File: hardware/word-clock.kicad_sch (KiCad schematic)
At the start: 0 parts

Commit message: feat(hardware): schematic v0 - erc clean, ready for pcb layout
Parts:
- added C2, C3, C4, C5, C6: 100nF, symbol Device:C
- added C7: 1000µF / 10V, symbol Device:C_Polarized
- added ESP32: ESP32 DevKit V1, symbol Connector_Generic:Conn_02x19_Odd_Even
- added J_AMP1: MAX98357A breakout, symbol Connector_Generic:Conn_01x07
- added J_LED1: WS2812B strip, symbol Connector_Generic:Conn_01x03
- added J_RTC1: DS3231 ZS-042, symbol Connector_Generic:Conn_01x06
- added J_SD1: HW-125 microSD, symbol Connector_Generic:Conn_01x06
- added J_USB1: USB-C breakout (Cermant 16P), symbol Connector_Generic:Conn_01x04
- added R1: Resistor 300 ohm, symbol Device:R
- added SW1: Hour, symbol Switch:SW_Push
- added SW2: Minute, symbol Switch:SW_Push
- added SW3: Audio, symbol Switch:SW_Push
- added U2: 74HC245, symbol 74xx:74HC245
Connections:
- new net +3V3: C2.1, C5.1, ESP32.3V3, J_RTC1.5 (VCC)
- new net +5V: C3.1, C4.2, C6.2, C7.1, ESP32.VIN (Pin_19), J_AMP1.7 (VIN), J_LED1.1 (+5V), J_SD1.2 (VCC), J_USB1.1 (VBUS), U2.1 (A->B), U2.20 (VCC)
- new net BTN_AUDIO: ESP32.D14 (Pin_12), SW3.1
- new net BTN_HOUR: ESP32.D32 (Pin_7), SW1.1
- new net BTN_MINUTE: ESP32.D33 (Pin_8), SW2.1
- new net GND: C2.2, C3.2, C4.1, C5.2, C6.1, C7.2, ESP32.GND (Pin_26), J_AMP1.6 (GND), J_LED1.2 (GND), J_RTC1.6 (GND), J_SD1.1 (GND), J_USB1.2 (GND), SW1.2, SW2.2, SW3.2, U2.10 (GND), U2.19 (CE), U2.3 (A1), U2.4 (A2), U2.5 (A3), U2.6 (A4), U2.7 (A5), U2.8 (A6), U2.9 (A7)
- new net I2C_SCL: ESP32.D22 (Pin_22), J_RTC1.3 (SCL)
- new net I2C_SDA: ESP32.D21 (Pin_25), J_RTC1.4 (SDA)
- new net I2S_BCLK: ESP32.D26 (Pin_10), J_AMP1.2 (BCLK)
- new net I2S_DIN: ESP32.D27 (Pin_11), J_AMP1.3 (DIN)
- new net I2S_LRC: ESP32.D25 (Pin_9), J_AMP1.1 (LRC)
- new net LED_DATA_3V3: ESP32.D13 (Pin_15), U2.2 (A0)
- new net LED_DATA_5V: R1.1, U2.18 (B0)
- new net LED_DATA_OUT: J_LED1.3 (DATA), R1.2
- new net SD_CS: ESP32.D5 (Pin_29), J_SD1.6 (CS)
- new net SD_MISO: ESP32.D19 (Pin_27), J_SD1.3 (MISO)
- new net SD_MOSI: ESP32.D23 (Pin_21), J_SD1.4 (MOSI)
- new net SD_SCK: ESP32.D18 (Pin_28), J_SD1.5 (SCK)
- no-connect marks 0 -> 33

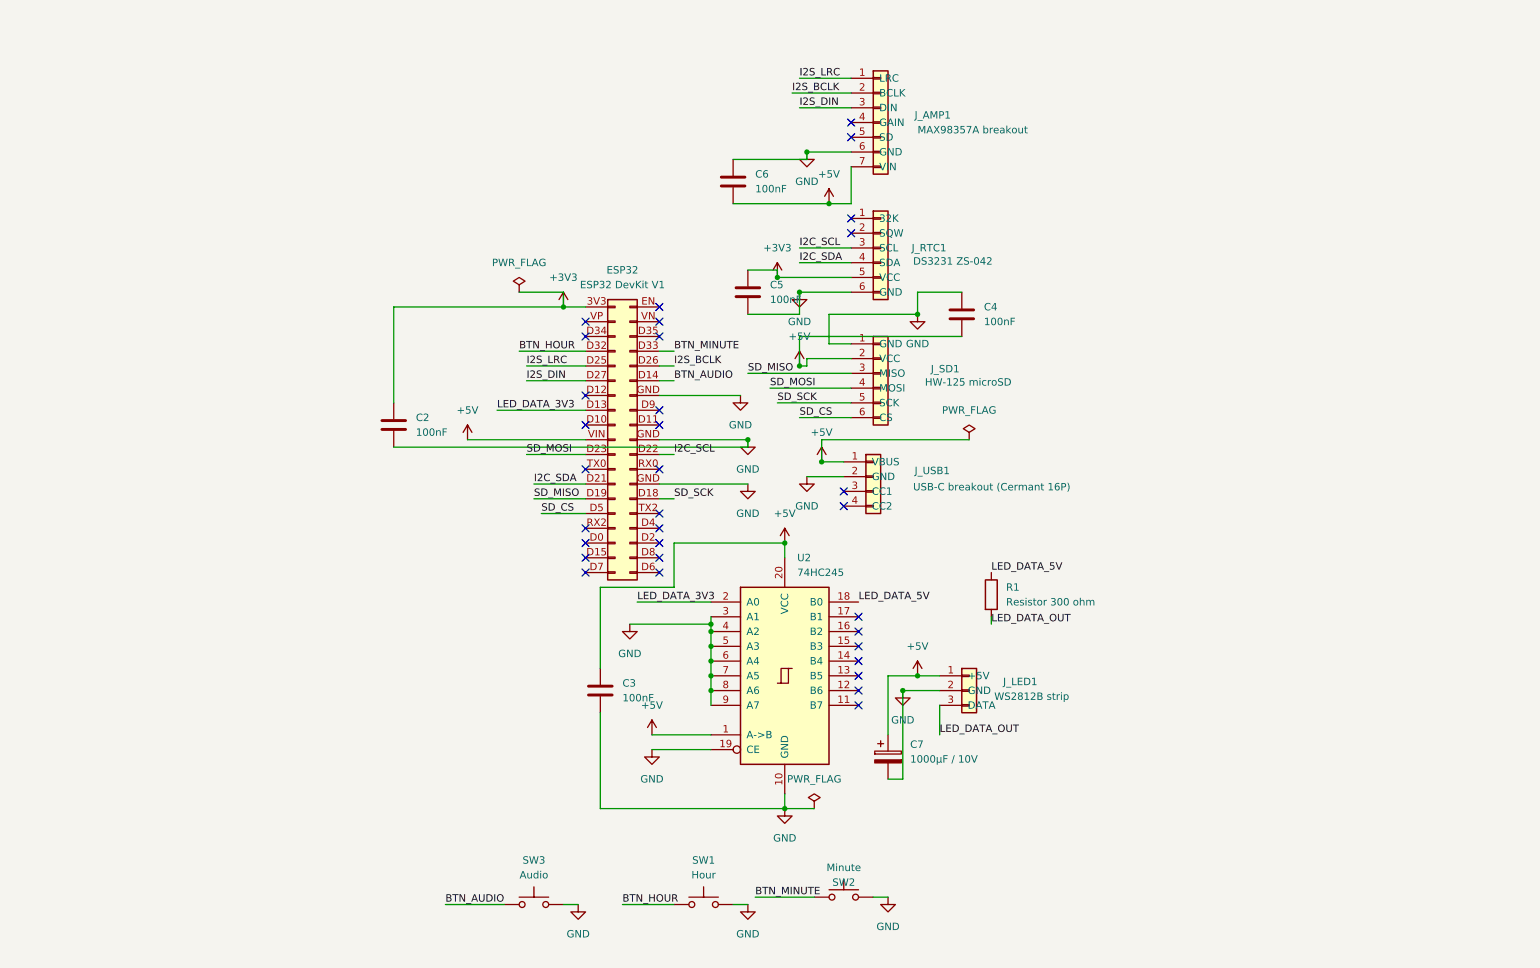
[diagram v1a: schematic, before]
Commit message: feat(hardware): schematic — 35 smd ws2812b leds chained
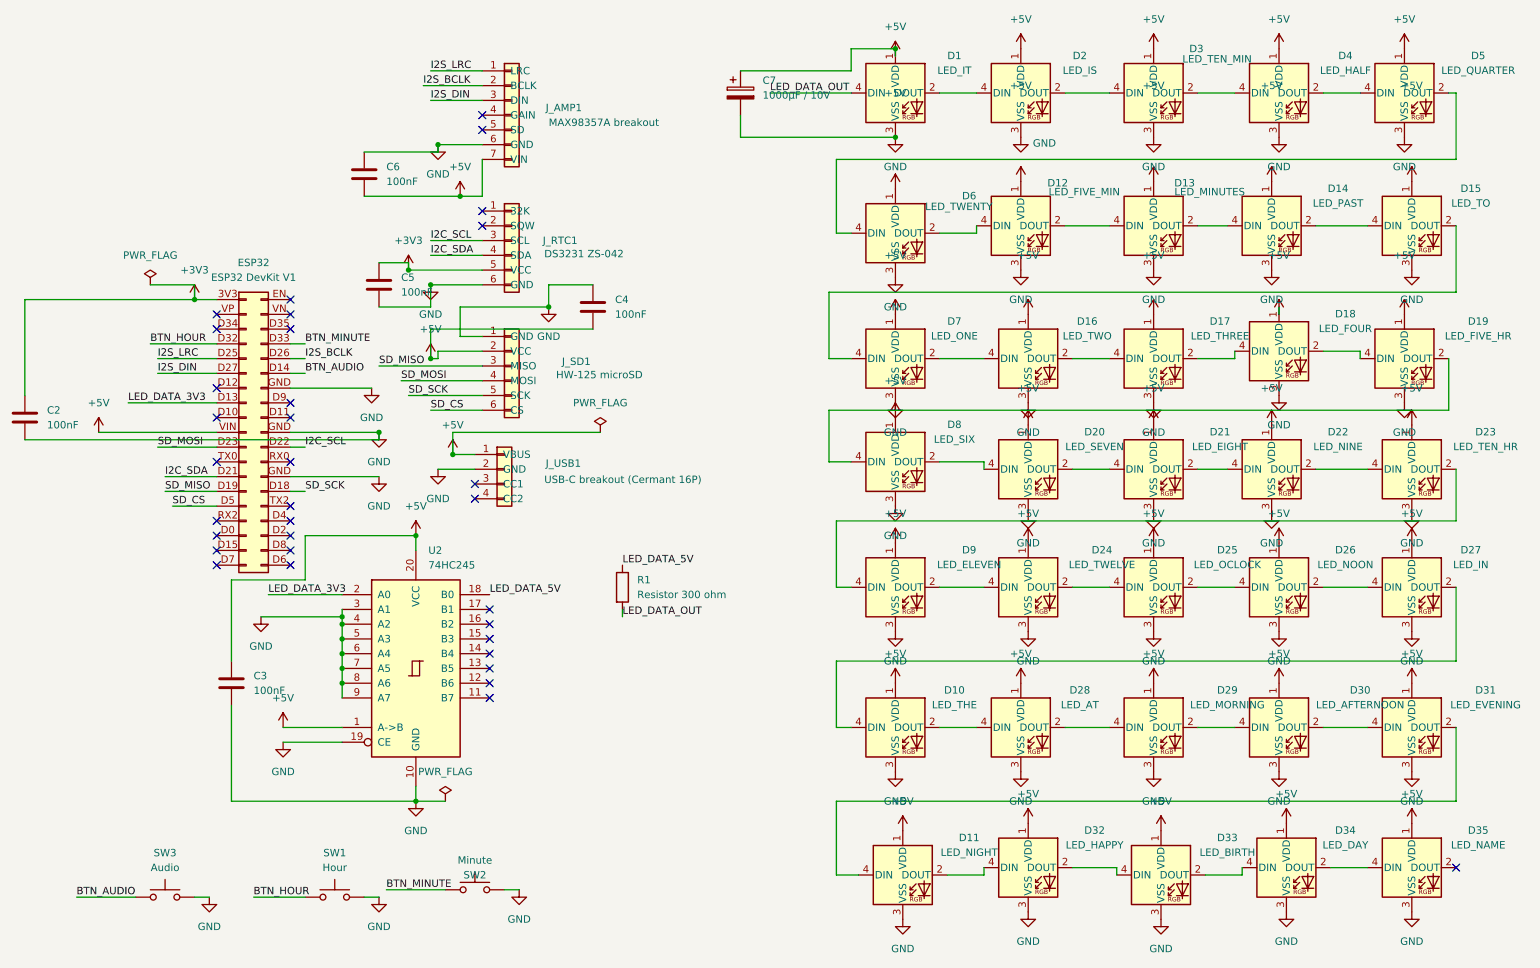
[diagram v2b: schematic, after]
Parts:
- removed J_LED1: WS2812B strip, symbol Connector_Generic:Conn_01x03
- added D1: LED_IT, LED_SMD:LED_WS2812B_PLCC4_5.0x5.0mm_P3.2mm, symbol LED:WS2812B
- added D10: LED_THE, LED_SMD:LED_WS2812B_PLCC4_5.0x5.0mm_P3.2mm, symbol LED:WS2812B
- added D11: LED_NIGHT, LED_SMD:LED_WS2812B_PLCC4_5.0x5.0mm_P3.2mm, symbol LED:WS2812B
- added D12: LED_FIVE_MIN, LED_SMD:LED_WS2812B_PLCC4_5.0x5.0mm_P3.2mm, symbol LED:WS2812B
- added D13: LED_MINUTES, LED_SMD:LED_WS2812B_PLCC4_5.0x5.0mm_P3.2mm, symbol LED:WS2812B
- added D14: LED_PAST, LED_SMD:LED_WS2812B_PLCC4_5.0x5.0mm_P3.2mm, symbol LED:WS2812B
- added D15: LED_TO, LED_SMD:LED_WS2812B_PLCC4_5.0x5.0mm_P3.2mm, symbol LED:WS2812B
- added D16: LED_TWO, LED_SMD:LED_WS2812B_PLCC4_5.0x5.0mm_P3.2mm, symbol LED:WS2812B
- added D17: LED_THREE, LED_SMD:LED_WS2812B_PLCC4_5.0x5.0mm_P3.2mm, symbol LED:WS2812B
- added D18: LED_FOUR, LED_SMD:LED_WS2812B_PLCC4_5.0x5.0mm_P3.2mm, symbol LED:WS2812B
- added D19: LED_FIVE_HR, LED_SMD:LED_WS2812B_PLCC4_5.0x5.0mm_P3.2mm, symbol LED:WS2812B
- added D2: LED_IS, LED_SMD:LED_WS2812B_PLCC4_5.0x5.0mm_P3.2mm, symbol LED:WS2812B
- added D20: LED_SEVEN, LED_SMD:LED_WS2812B_PLCC4_5.0x5.0mm_P3.2mm, symbol LED:WS2812B
- added D21: LED_EIGHT, LED_SMD:LED_WS2812B_PLCC4_5.0x5.0mm_P3.2mm, symbol LED:WS2812B
- added D22: LED_NINE, LED_SMD:LED_WS2812B_PLCC4_5.0x5.0mm_P3.2mm, symbol LED:WS2812B
- added D23: LED_TEN_HR, LED_SMD:LED_WS2812B_PLCC4_5.0x5.0mm_P3.2mm, symbol LED:WS2812B
- added D24: LED_TWELVE, LED_SMD:LED_WS2812B_PLCC4_5.0x5.0mm_P3.2mm, symbol LED:WS2812B
- added D25: LED_OCLOCK, LED_SMD:LED_WS2812B_PLCC4_5.0x5.0mm_P3.2mm, symbol LED:WS2812B
- added D26: LED_NOON, LED_SMD:LED_WS2812B_PLCC4_5.0x5.0mm_P3.2mm, symbol LED:WS2812B
- added D27: LED_IN, LED_SMD:LED_WS2812B_PLCC4_5.0x5.0mm_P3.2mm, symbol LED:WS2812B
- added D28: LED_AT, LED_SMD:LED_WS2812B_PLCC4_5.0x5.0mm_P3.2mm, symbol LED:WS2812B
- added D29: LED_MORNING, LED_SMD:LED_WS2812B_PLCC4_5.0x5.0mm_P3.2mm, symbol LED:WS2812B
- added D3: LED_TEN_MIN, LED_SMD:LED_WS2812B_PLCC4_5.0x5.0mm_P3.2mm, symbol LED:WS2812B
- added D30: LED_AFTERNOON, LED_SMD:LED_WS2812B_PLCC4_5.0x5.0mm_P3.2mm, symbol LED:WS2812B
- added D31: LED_EVENING, LED_SMD:LED_WS2812B_PLCC4_5.0x5.0mm_P3.2mm, symbol LED:WS2812B
- added D32: LED_HAPPY, LED_SMD:LED_WS2812B_PLCC4_5.0x5.0mm_P3.2mm, symbol LED:WS2812B
- added D33: LED_BIRTH, LED_SMD:LED_WS2812B_PLCC4_5.0x5.0mm_P3.2mm, symbol LED:WS2812B
- added D34: LED_DAY, LED_SMD:LED_WS2812B_PLCC4_5.0x5.0mm_P3.2mm, symbol LED:WS2812B
- added D35: LED_NAME, LED_SMD:LED_WS2812B_PLCC4_5.0x5.0mm_P3.2mm, symbol LED:WS2812B
- added D4: LED_HALF, LED_SMD:LED_WS2812B_PLCC4_5.0x5.0mm_P3.2mm, symbol LED:WS2812B
- added D5: LED_QUARTER, LED_SMD:LED_WS2812B_PLCC4_5.0x5.0mm_P3.2mm, symbol LED:WS2812B
- added D6: LED_TWENTY, LED_SMD:LED_WS2812B_PLCC4_5.0x5.0mm_P3.2mm, symbol LED:WS2812B
- added D7: LED_ONE, LED_SMD:LED_WS2812B_PLCC4_5.0x5.0mm_P3.2mm, symbol LED:WS2812B
- added D8: LED_SIX, LED_SMD:LED_WS2812B_PLCC4_5.0x5.0mm_P3.2mm, symbol LED:WS2812B
- added D9: LED_ELEVEN, LED_SMD:LED_WS2812B_PLCC4_5.0x5.0mm_P3.2mm, symbol LED:WS2812B
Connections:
- net +5V: now also D1.1 (VDD), D10.1 (VDD), D11.1 (VDD), D12.1 (VDD), D13.1 (VDD), D14.1 (VDD), D15.1 (VDD), D16.1 (VDD), D17.1 (VDD), D18.1 (VDD), D19.1 (VDD), D2.1 (VDD), D20.1 (VDD), D21.1 (VDD), D22.1 (VDD), D23.1 (VDD), D24.1 (VDD), D25.1 (VDD), D26.1 (VDD), D27.1 (VDD), D28.1 (VDD), D29.1 (VDD), D3.1 (VDD), D30.1 (VDD), D31.1 (VDD), D32.1 (VDD), D33.1 (VDD), D34.1 (VDD), D35.1 (VDD), D4.1 (VDD), D5.1 (VDD), D6.1 (VDD), D7.1 (VDD), D8.1 (VDD), D9.1 (VDD)
- net GND: now also D1.3 (VSS), D10.3 (VSS), D11.3 (VSS), D12.3 (VSS), D13.3 (VSS), D14.3 (VSS), D15.3 (VSS), D16.3 (VSS), D17.3 (VSS), D18.3 (VSS), D19.3 (VSS), D2.3 (VSS), D20.3 (VSS), D21.3 (VSS), D22.3 (VSS), D23.3 (VSS), D24.3 (VSS), D25.3 (VSS), D26.3 (VSS), D27.3 (VSS), D28.3 (VSS), D29.3 (VSS), D3.3 (VSS), D30.3 (VSS), D31.3 (VSS), D32.3 (VSS), D33.3 (VSS), D34.3 (VSS), D35.3 (VSS), D4.3 (VSS), D5.3 (VSS), D6.3 (VSS), D7.3 (VSS), D8.3 (VSS), D9.3 (VSS)
- net LED_DATA_OUT: now also D1.4 (DIN)
- new net: D19.2 (DOUT), D8.4 (DIN)
- new net: D18.2 (DOUT), D19.4 (DIN)
- new net: D13.2 (DOUT), D14.4 (DIN)
- new net: D12.2 (DOUT), D13.4 (DIN)
- new net: D24.2 (DOUT), D25.4 (DIN)
- new net: D24.4 (DIN), D9.2 (DOUT)
- new net: D26.2 (DOUT), D27.4 (DIN)
- new net: D25.2 (DOUT), D26.4 (DIN)
- new net: D12.4 (DIN), D6.2 (DOUT)
- new net: D17.2 (DOUT), D18.4 (DIN)
- new net: D16.2 (DOUT), D17.4 (DIN)
- new net: D14.2 (DOUT), D15.4 (DIN)
- new net: D34.2 (DOUT), D35.4 (DIN)
- new net: D33.2 (DOUT), D34.4 (DIN)
- new net: D4.2 (DOUT), D5.4 (DIN)
- new net: D3.2 (DOUT), D4.4 (DIN)
- new net: D5.2 (DOUT), D6.4 (DIN)
- new net: D30.2 (DOUT), D31.4 (DIN)
- new net: D29.2 (DOUT), D30.4 (DIN)
- new net: D15.2 (DOUT), D7.4 (DIN)
- new net: D11.2 (DOUT), D32.4 (DIN)
- new net: D11.4 (DIN), D31.2 (DOUT)
- new net: D23.2 (DOUT), D9.4 (DIN)
- new net: D22.2 (DOUT), D23.4 (DIN)
- new net: D10.2 (DOUT), D28.4 (DIN)
- new net: D10.4 (DIN), D27.2 (DOUT)
- new net: D21.2 (DOUT), D22.4 (DIN)
- new net: D28.2 (DOUT), D29.4 (DIN)
- new net: D1.2 (DOUT), D2.4 (DIN)
- new net: D20.2 (DOUT), D21.4 (DIN)
- new net: D20.4 (DIN), D8.2 (DOUT)
- new net: D16.4 (DIN), D7.2 (DOUT)
- new net: D32.2 (DOUT), D33.4 (DIN)
- new net: D2.2 (DOUT), D3.4 (DIN)
- no-connect marks 33 -> 34
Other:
- moved on the sheet: C2, C3, C4, C5, C6, C7, ESP32, J_AMP1, J_RTC1, J_SD1, J_USB1, R1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

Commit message: feat(hardware): footprints assigned; esp32 swif7ify library added
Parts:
- C2, C3, C4, C5, C6: footprint (none) -> Capacitor_THT:C_Disc_D5.0mm_W2.5mm_P5.00mm
- C7: footprint (none) -> Capacitor_THT:CP_Radial_D10.0mm_P5.00mm
- ESP32: footprint (none) -> ESP32_DevKit_V1:ESP32_38Pin
- J_AMP1: footprint (none) -> Connector_PinHeader_2.54mm:PinHeader_1x07_P2.54mm_Vertical
- J_RTC1, J_SD1: footprint (none) -> Connector_PinHeader_2.54mm:PinHeader_1x06_P2.54mm_Vertical
- J_USB1: footprint (none) -> Connector_PinHeader_2.54mm:PinHeader_1x16_P2.54mm_Vertical
- R1: footprint (none) -> Resistor_THT:R_Axial_DIN0207_L6.3mm_D2.5mm_P10.16mm_Horizontal
- SW1, SW2, SW3: footprint (none) -> Button_Switch_THT:SW_PUSH_6mm
- U2: footprint (none) -> Package_DIP:DIP-20_W7.62mm
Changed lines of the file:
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@@
 			)
 		)
-		(property "Footprint" ""
+		(property "Footprint" "Connector_PinHeader_2.54mm:PinHeader_1x07_P2.54mm_Vertical"
 			(at 104.14 26.67 0)
 			(hide yes)
@@
 			)
 		)
-		(property "Footprint" ""
+		(property "Footprint" "ESP32_DevKit_V1:ESP32_38Pin"
 			(at 58.42 81.28 0)
 			(hide yes)
@@
 			)
 		)
-		(property "Footprint" ""
+		(property "Footprint" "Connector_PinHeader_2.54mm:PinHeader_1x06_P2.54mm_Vertical"
 			(at 104.14 69.85 0)
 			(hide yes)
@@
 			)
 		)
-		(property "Footprint" ""
+		(property "Footprint" "Capacitor_THT:CP_Radial_D10.0mm_P5.00mm"
 			(at 144.4752 26.67 0)
 			(hide yes)
@@
 			)
 		)
-		(property "Footprint" ""
+		(property "Footprint" "Button_Switch_THT:SW_PUSH_6mm"
 			(at 44.45 156.21 0)
 			(hide yes)
@@
 			)
 		)
-		(property "Footprint" ""
+		(property "Footprint" "Connector_PinHeader_2.54mm:PinHeader_1x06_P2.54mm_Vertical"
 			(at 104.14 48.26 0)
 			(hide yes)
@@
 			)
 		)
-		(property "Footprint" ""
+		(property "Footprint" "Capacitor_THT:C_Disc_D5.0mm_W2.5mm_P5.00mm"
 			(at 21.2852 82.55 0)
 			(hide yes)
@@
 			)
 		)
-		(property "Footprint" ""
+		(property "Footprint" "Connector_PinHeader_2.54mm:PinHeader_1x16_P2.54mm_Vertical"
 			(at 102.87 87.63 0)
 			(hide yes)
@@
 			)
 		)
-		(property "Footprint" ""
+		(property "Footprint" "Package_DIP:DIP-20_W7.62mm"
 			(at 87.63 121.92 0)
 			(hide yes)
@@
 			)
 		)
-		(property "Footprint" ""
+		(property "Footprint" "Capacitor_THT:C_Disc_D5.0mm_W2.5mm_P5.00mm"
 			(at 82.2452 59.69 0)
 			(hide yes)
@@
 			)
 		)
-		(property "Footprint" ""
+		(property "Footprint" "Capacitor_THT:C_Disc_D5.0mm_W2.5mm_P5.00mm"
 			(at 119.0752 63.5 0)
 			(hide yes)
@@
 			)
 		)
-		(property "Footprint" ""
+		(property "Footprint" "Button_Switch_THT:SW_PUSH_6mm"
 			(at 73.66 156.21 0)
 			(hide yes)
@@
 			)
 		)
-		(property "Footprint" ""
+		(property "Footprint" "Capacitor_THT:C_Disc_D5.0mm_W2.5mm_P5.00mm"
 			(at 79.7052 40.64 0)
 			(hide yes)
@@
 			)
 		)
-		(property "Footprint" ""
+		(property "Footprint" "Capacitor_THT:C_Disc_D5.0mm_W2.5mm_P5.00mm"
 			(at 56.8452 128.27 0)
 			(hide yes)
@@
 			)
 		)
-		(property "Footprint" ""
+		(property "Footprint" "Button_Switch_THT:SW_PUSH_6mm"
 			(at 97.79 154.94 0)
 			(hide yes)
@@
 			)
 		)
-		(property "Footprint" ""
+		(property "Footprint" "Resistor_THT:R_Axial_DIN0207_L6.3mm_D2.5mm_P10.16mm_Horizontal"
 			(at 121.412 107.95 90)
 			(hide yes)

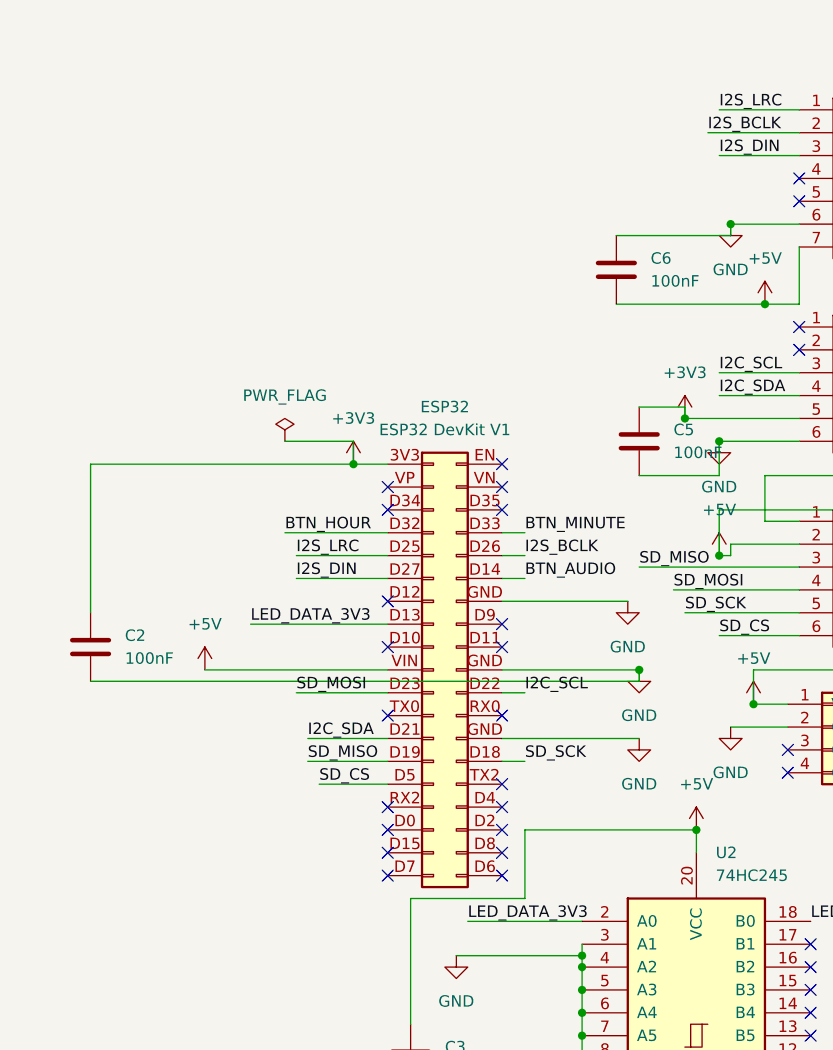
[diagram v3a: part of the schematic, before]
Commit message: feat(hardware): phase 3 pcb component placement complete
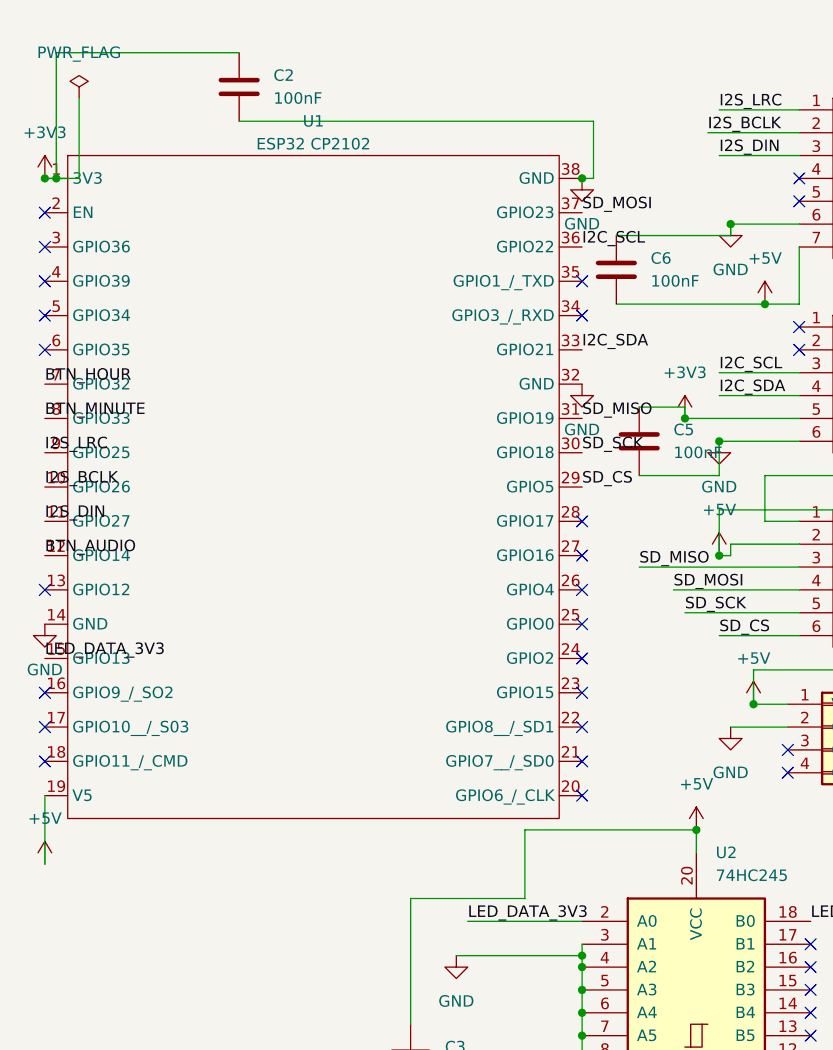
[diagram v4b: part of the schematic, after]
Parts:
- removed ESP32: ESP32 DevKit V1, ESP32_DevKit_V1:ESP32_38Pin, symbol Connector_Generic:Conn_02x19_Odd_Even
- added U1: ESP32 CP2102, ESP32_DevKit_V1:ESP32_38Pin, symbol Swif7ify:ESP32_38Pin_Symbol
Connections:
- net +3V3: now also U1.1 (3V3)
- net +5V: now also U1.19 (V5)
- net BTN_AUDIO: now also U1.12 (GPIO14)
- net BTN_HOUR: now also U1.7 (GPIO32)
- net BTN_MINUTE: now also U1.8 (GPIO33)
- net GND: now also U1.14 (GND), U1.32 (GND), U1.38 (GND)
- net I2C_SCL: now also U1.36 (GPIO22)
- net I2C_SDA: now also U1.33 (GPIO21)
- net I2S_BCLK: now also U1.10 (GPIO26)
- net I2S_DIN: now also U1.11 (GPIO27)
- net I2S_LRC: now also U1.9 (GPIO25)
- net LED_DATA_3V3: now also U1.15 (GPIO13)
- net SD_CS: now also U1.29 (GPIO5)
- net SD_MISO: now also U1.31 (GPIO19)
- net SD_MOSI: now also U1.37 (GPIO23)
- net SD_SCK: now also U1.30 (GPIO18)
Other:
- moved on the sheet: C2
